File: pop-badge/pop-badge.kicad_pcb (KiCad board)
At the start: 2 copper layers, 129.5 x 101.3 mm, 164 parts, among them J1 Conn_01x05, Q1 S9013, Q2 AO3400A, U1 WS2812-2020, U10 WS2812-2020, U11 WS2812-2020, U12 WS2812-2020, U13 WS2812-2020, U14 WS2812-2020, U15 WS2812-2020, U16 WS2812-2020, U17 WS2812-2020, U18 WS2812-2020, U19 WS2812-2020, U2 WS2812-2020, U20 WS2812-2020, U21 WS2812-2020, U22 WS2812-2020, U23 WS2812-2020, U24 WS2812-2020, U25 WS2812-2020, U26 Pico, U3 WS2812-2020, U4 WS2812-2020, U5 WS2812-2020, U6 WS2812-2020, U7 WS2812-2020, U8 WS2812-2020, U9 WS2812-2020

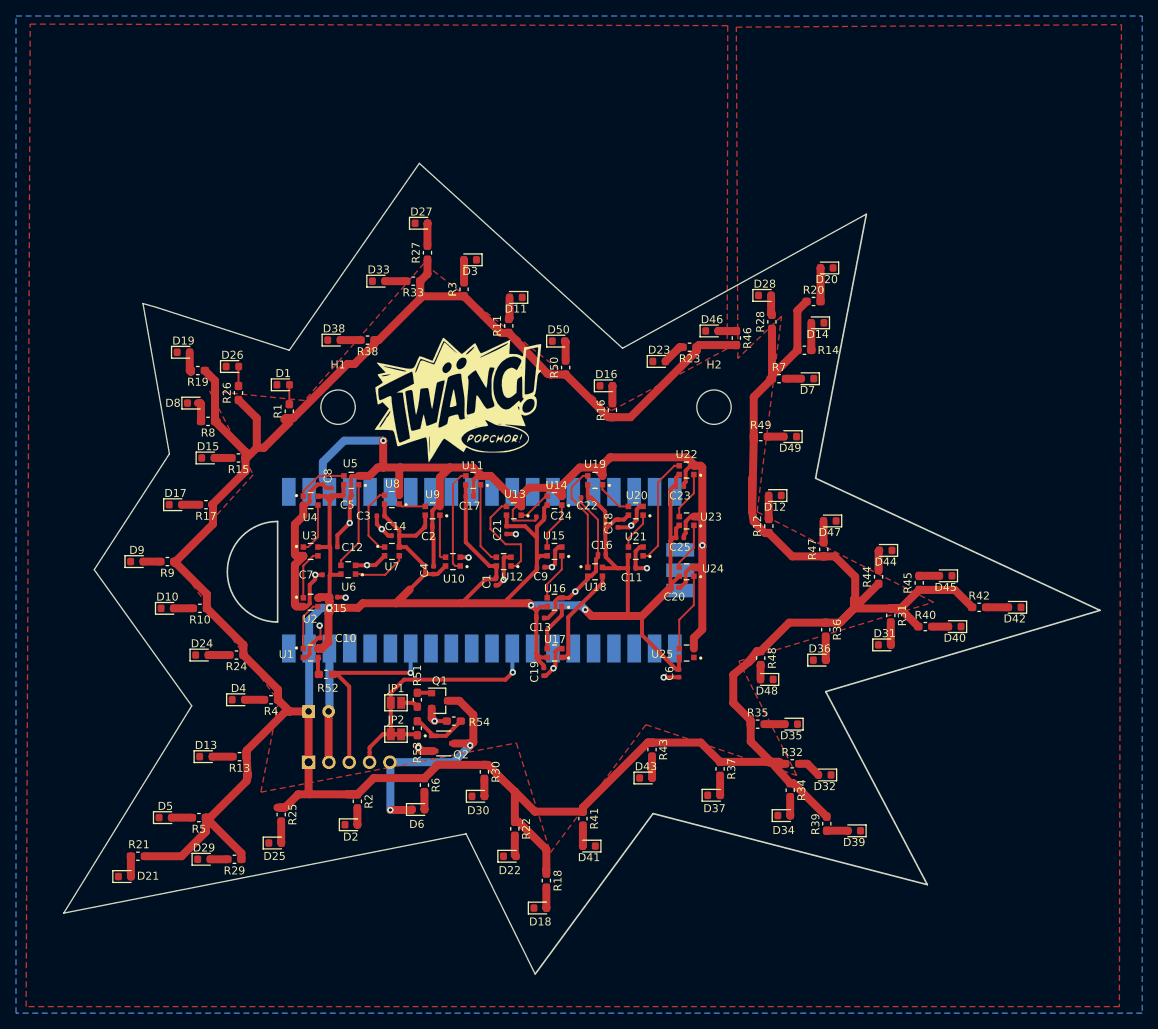
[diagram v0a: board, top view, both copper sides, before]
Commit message: add button
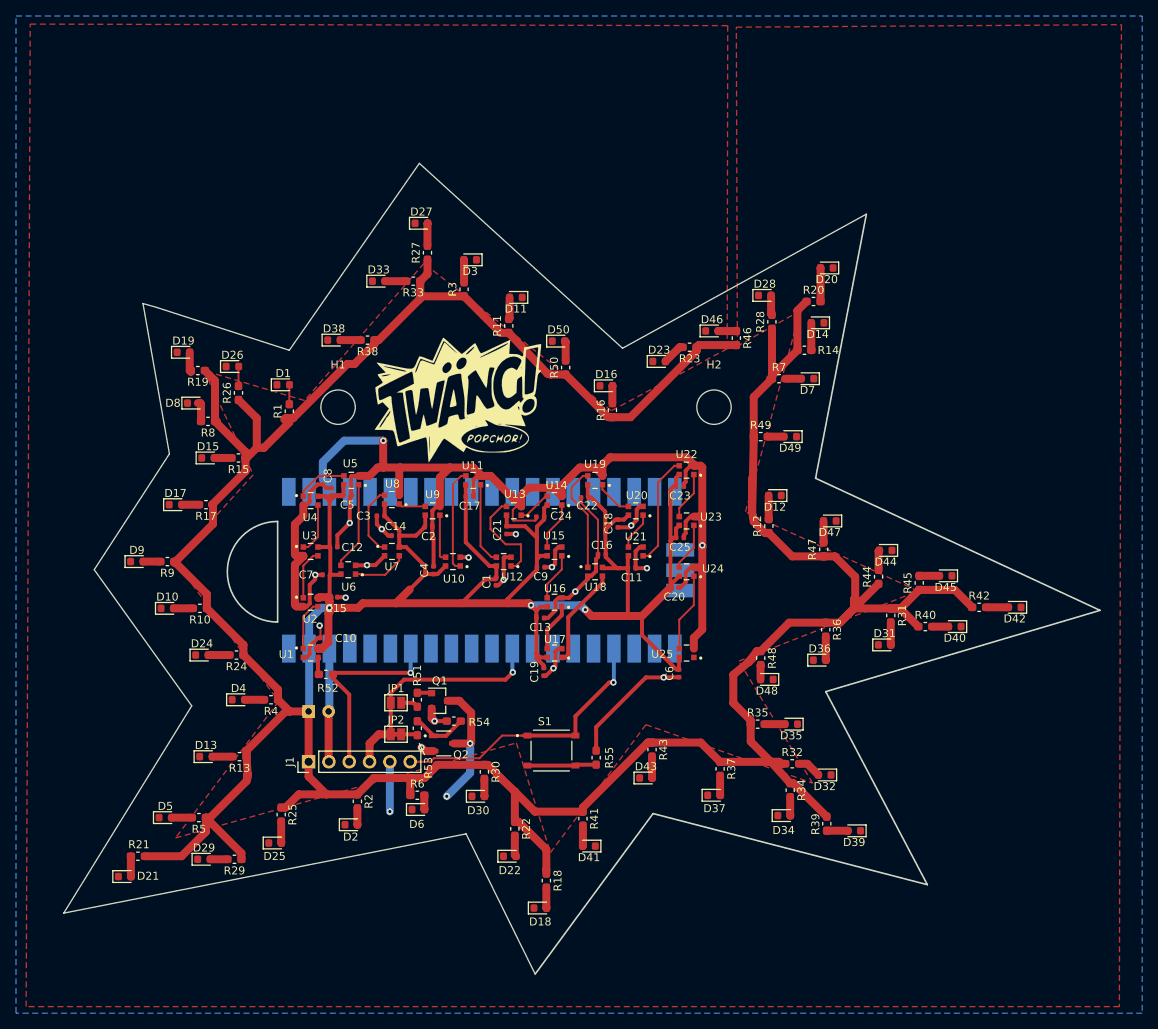
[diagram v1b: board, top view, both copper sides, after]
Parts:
- added R55: 200, Resistor_SMD:R_0603_1608Metric_Pad1.05x0.95mm_HandSolder, F.Cu at (80.5, 116.2)
- added S1: TS-1187A-B-A-B, footprints:SW_TS-1187A-B-A-B, F.Cu at (74.9, 115.3)
- J1: value Conn_01x05 -> Conn_01x06; footprint Connector_PinSocket_2.54mm:PinSocket_1x05_P2.54mm_Vertical -> Connector_PinHeader_2.54mm:PinHeader_1x06_P2.54mm_Vertical; moved to F.Cu
- Raspberry Pi Pico: renamed from U26
- moved R6 1.55 mm to (58.2, 120.9), turned to 0 degrees
- moved J1 0.06 mm to (44.6, 116.7), turned to 90 degrees
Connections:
- Raspberry Pi Pico pad 24: Net-(U26-Pad24) -> Button
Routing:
- net Button: track 0.00 -> 36.8 mm, vias 0 -> 1
- net GND: track 248.7 -> 262.8 mm
- net Net-(R55-Pad1): track 0.00 -> 8.63 mm
- net LEDw-: track 29.7 -> 23.5 mm, vias 2 -> 3
- net +5V: track 642.3 -> 644.1 mm
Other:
- board text added: "Button"
- board text added: "jlcjlcjlcjlcjlcjlc"

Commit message: some cosmetic changes
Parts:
- U26: renamed from Raspberry Pi Pico
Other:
- board text added: "JLCJLCJLCJLC"
- board text removed: "jlcjlcjlcjlcjlcjlc"
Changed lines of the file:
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@@
     (tags "Through hole pin header THT 2x20 2.54mm double row")
     (attr smd)
-    (fp_text reference "Raspberry Pi Pico" (at -0.9525 -14.1605 180) (layer B.SilkS)
+    (fp_text reference U26 (at -0.9525 -14.1605 180) (layer B.SilkS)
       (effects (font (size 1 1) (thickness 0.15)) (justify mirror))
     )
@@
     )
   )
-  (gr_text jlcjlcjlcjlcjlcjlc (at 51.181 89.916) (layer B.SilkS)
+  (gr_text JLCJLCJLCJLC (at 51.181 89.916) (layer B.SilkS)
     (effects (font (size 1 1) (thickness 0.15)) (justify mirror))
   )

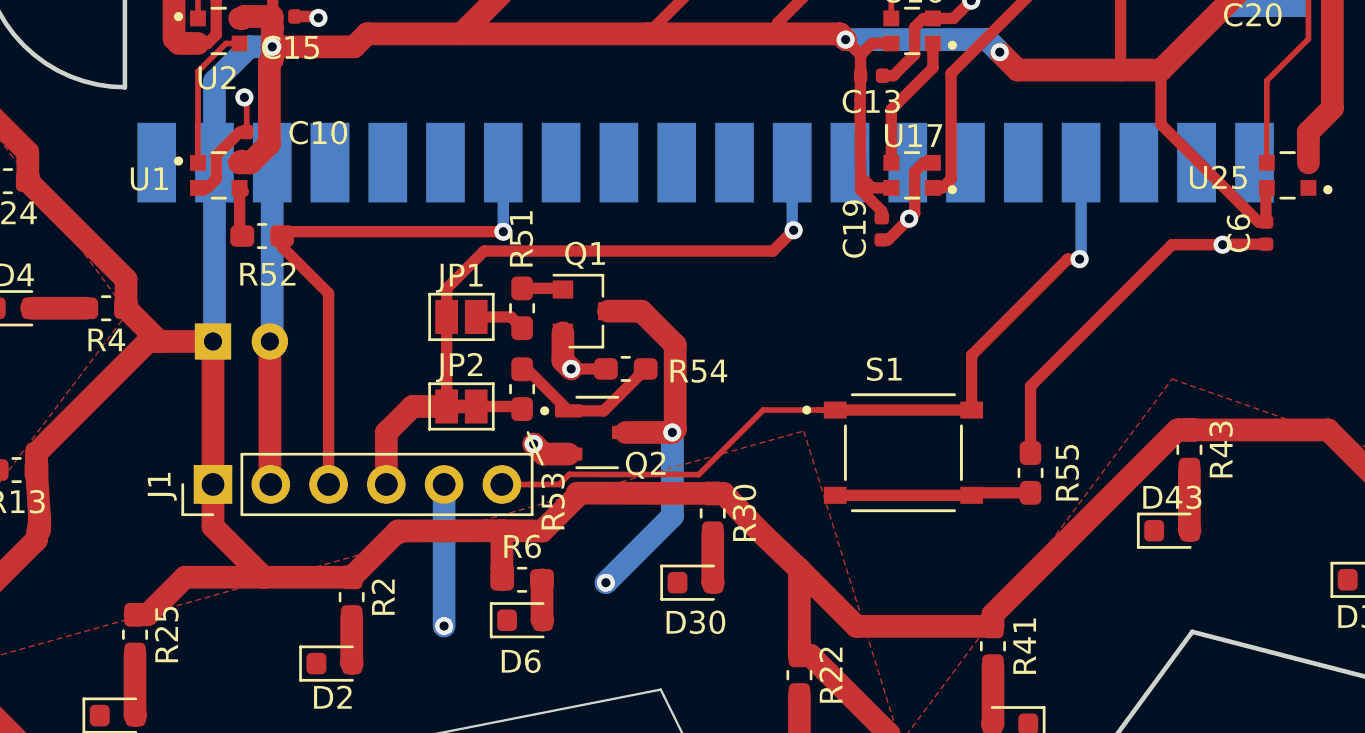
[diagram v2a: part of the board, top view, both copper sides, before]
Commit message: remove button again
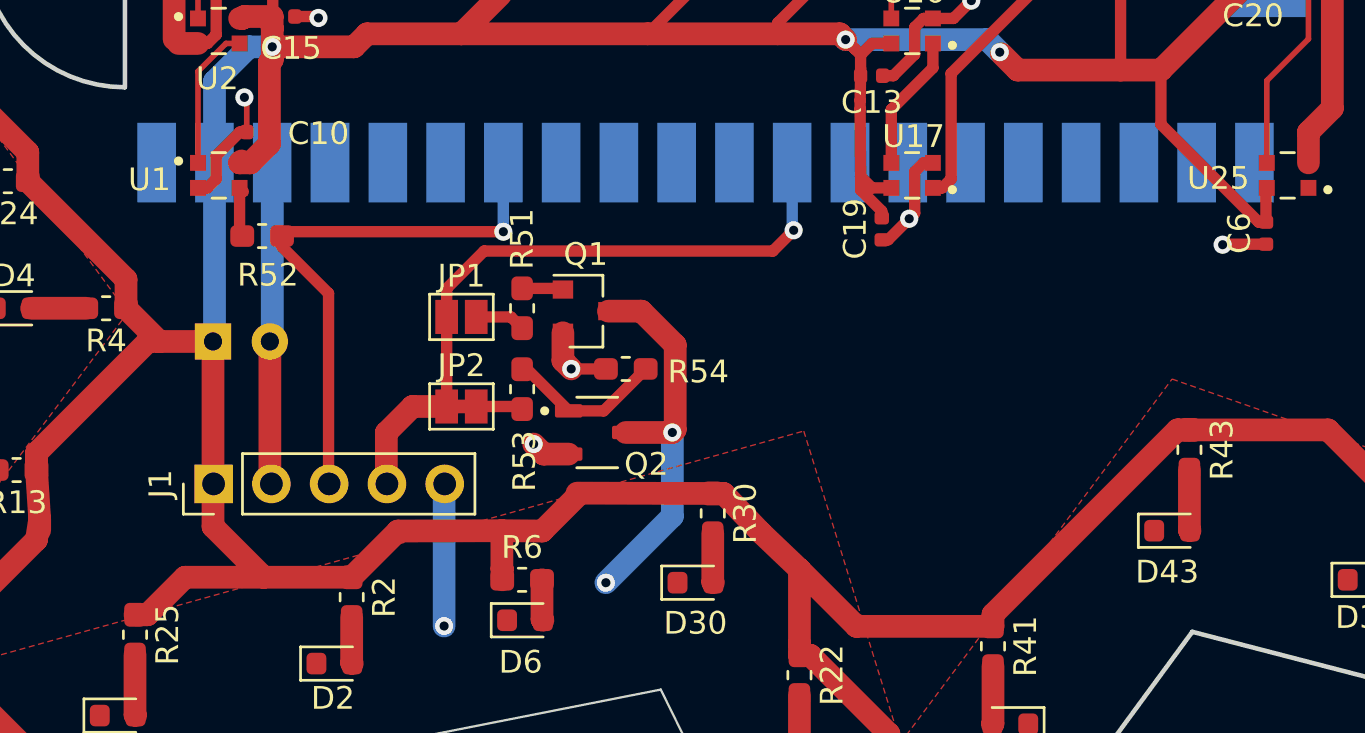
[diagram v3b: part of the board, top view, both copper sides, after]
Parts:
- removed R55: 200, Resistor_SMD:R_0603_1608Metric_Pad1.05x0.95mm_HandSolder
- removed S1: TS-1187A-B-A-B, footprints:SW_TS-1187A-B-A-B
- J1: value Conn_01x06 -> Conn_01x05; footprint Connector_PinHeader_2.54mm:PinHeader_1x06_P2.54mm_Vertical -> Connector_PinHeader_2.54mm:PinHeader_1x05_P2.54mm_Vertical
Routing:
- net Button: track 36.8 -> 0.00 mm, vias 1 -> 0
- net GND: track 262.8 -> 248.3 mm
- net Net-(R55-Pad1): track 8.63 -> 0.00 mm

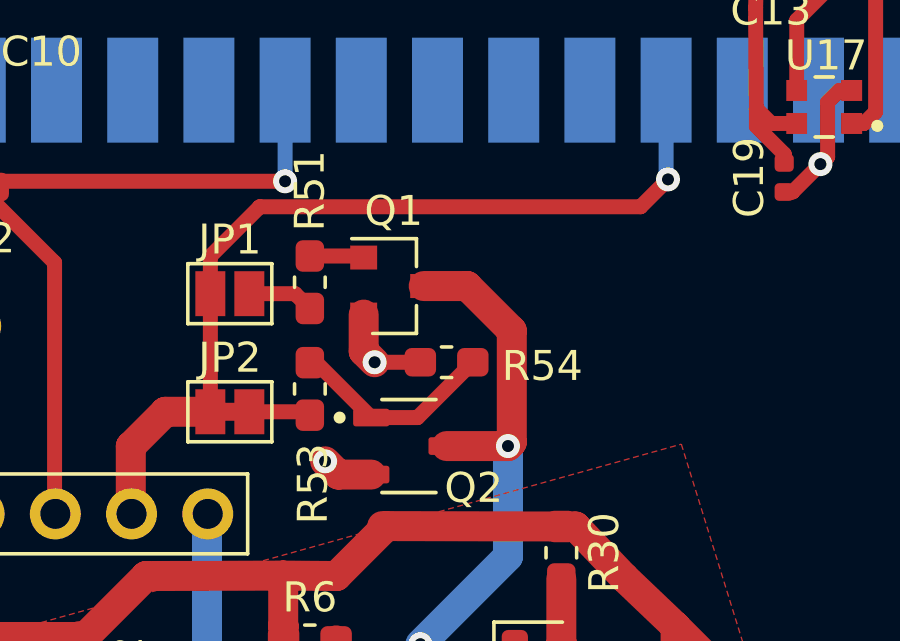
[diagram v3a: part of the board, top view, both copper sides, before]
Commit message: change footprint for npn slightly
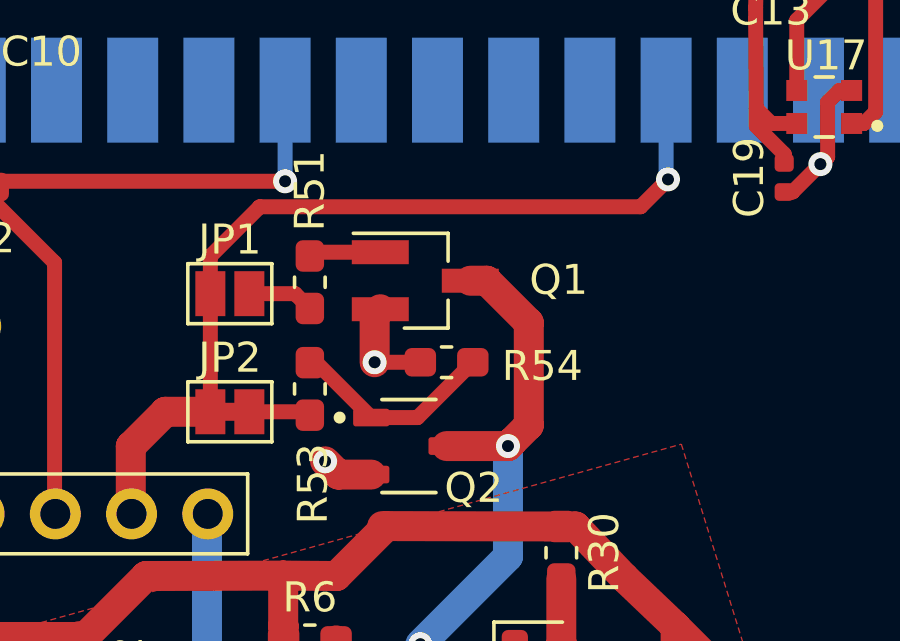
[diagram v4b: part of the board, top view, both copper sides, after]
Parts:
- Q1: footprint Package_TO_SOT_SMD:SOT-23 -> Package_TO_SOT_SMD:SOT-23_Handsoldering
- moved Q1 1.07 mm to (62.0, 108.9)
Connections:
- net Button renamed Net-(U26-Pad24)
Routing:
- net Net-(Q1-Pad1): track 1.82 -> 2.40 mm
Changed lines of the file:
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@@
     (thickness 1.6)
     (drawings 27)
-    (tracks 736)
+    (tracks 737)
     (zones 0)
     (modules 164)
@@
     (47 F.CrtYd user)
     (48 B.Fab user)
-    (49 F.Fab user)
+    (49 F.Fab user hide)
   )
   (setup
-    (last_trace_width 1)
+    (last_trace_width 0.5)
     (user_trace_width 0.25)
     (user_trace_width 0.5)
@@
   (net 121 "Net-(JP2-Pad2)")
   (net 122 "Net-(Q2-Pad1)")
-  (net 123 Button)
+  (net 123 "Net-(U26-Pad24)")
   (net_class Default "This is the default net class."
     (clearance 0.2)
@@
     (uvia_drill 0.1)
     (add_net +5V)
-    (add_net Button)
     (add_net DIN)
     (add_net GND)
@@
     (add_net "Net-(U26-Pad22)")
     (add_net "Net-(U26-Pad23)")
+    (add_net "Net-(U26-Pad24)")
     (add_net "Net-(U26-Pad25)")
     (add_net "Net-(U26-Pad26)")
@@
     (add_net "Net-(U8-Pad1)")
   )
+  (module Package_TO_SOT_SMD:SOT-23_Handsoldering (layer F.Cu)
+    (at 62.0141 108.9152)
+    (descr "SOT-23, Handsoldering")
+    (tags SOT-23)
+    (attr smd)
+    (fp_text reference Q1 (at 4.445 -0.0254) (layer F.SilkS)
+      (effects (font (size 1 1) (thickness 0.15)))
+    )
+    (fp_text value S9013 (at 0 2.5) (layer F.Fab)
+      (effects (font (size 1 1) (thickness 0.15)))
+    )
+    (fp_line (start 0.76 1.58) (end -0.7 1.58) (layer F.SilkS) (width 0.12))
+    (fp_line (start -0.7 1.52) (end 0.7 1.52) (layer F.Fab) (width 0.1))
+    (fp_line (start 0.7 -1.52) (end 0.7 1.52) (layer F.Fab) (width 0.1))
+    (fp_line (start -0.7 -0.95) (end -0.15 -1.52) (layer F.Fab) (width 0.1))
+    (fp_line (start -0.15 -1.52) (end 0.7 -1.52) (layer F.Fab) (width 0.1))
+    (fp_line (start -0.7 -0.95) (end -0.7 1.5) (layer F.Fab) (width 0.1))
+    (fp_line (start 0.76 -1.58) (end -2.4 -1.58) (layer F.SilkS) (width 0.12))
+    (fp_line (start -2.7 1.75) (end -2.7 -1.75) (layer F.CrtYd) (width 0.05))
+    (fp_line (start 2.7 1.75) (end -2.7 1.75) (layer F.CrtYd) (width 0.05))
+    (fp_line (start 2.7 -1.75) (end 2.7 1.75) (layer F.CrtYd) (width 0.05))
+    (fp_line (start -2.7 -1.75) (end 2.7 -1.75) (layer F.CrtYd) (width 0.05))
+    (fp_line (start 0.76 -1.58) (end 0.76 -0.65) (layer F.SilkS) (width 0.12))
+    (fp_line (start 0.76 1.58) (end 0.76 0.65) (layer F.SilkS) (width 0.12))
+    (fp_text user %R (at 0 0 90) (layer F.Fab)
+      (effects (font (size 0.5 0.5) (thickness 0.075)))
+    )
+    (pad 3 smd rect (at 1.5 0) (size 1.9 0.8) (layers F.Cu F.Paste F.Mask)
+      (net 2 LEDw-))
+    (pad 2 smd rect (at -1.5 0.95) (size 1.9 0.8) (layers F.Cu F.Paste F.Mask)
+      (net 32 GND))
+    (pad 1 smd rect (at -1.5 -0.95) (size 1.9 0.8) (layers F.Cu F.Paste F.Mask)
+      (net 34 "Net-(Q1-Pad1)"))
+    (model ${KISYS3DMOD}/Package_TO_SOT_SMD.3dshapes/SOT-23.wrl
+      (at (xyz 0 0 0))
+      (scale (xyz 1 1 1))
+      (rotate (xyz 0 0 0))
+    )
+  )
   (module Connector_PinHeader_2.54mm:PinHeader_1x05_P2.54mm_Vertical (layer F.Cu)
     (at 44.6024 116.6876 90)
@@
       (xy -1.88617 -7.717509) (xy -1.826686 -7.789334) (xy -1.737876 -7.733648)) (layer F.SilkS) (width 0.01))
   )
-  (module Package_TO_SOT_SMD:SOT-23 (layer F.Cu)
-    (at 60.96 109.093)
-    (descr "SOT-23, Standard")
-    (tags SOT-23)
-    (attr smd)
-    (fp_text reference Q1 (at 0 -2.5) (layer F.SilkS)
-      (effects (font (size 1 1) (thickness 0.15)))
-    )
-    (fp_text value S9013 (at 0 2.5) (layer F.Fab)
-      (effects (font (size 1 1) (thickness 0.15)))
-    )
-    (fp_line (start 0.76 1.58) (end -0.7 1.58) (layer F.SilkS) (width 0.12))
-    (fp_line (start 0.76 -1.58) (end -1.4 -1.58) (layer F.SilkS) (width 0.12))
-    (fp_line (start -1.7 1.75) (end -1.7 -1.75) (layer F.CrtYd) (width 0.05))
-    (fp_line (start 1.7 1.75) (end -1.7 1.75) (layer F.CrtYd) (width 0.05))
-    (fp_line (start 1.7 -1.75) (end 1.7 1.75) (layer F.CrtYd) (width 0.05))
-    (fp_line (start -1.7 -1.75) (end 1.7 -1.75) (layer F.CrtYd) (width 0.05))
-    (fp_line (start 0.76 -1.58) (end 0.76 -0.65) (layer F.SilkS) (width 0.12))
-    (fp_line (start 0.76 1.58) (end 0.76 0.65) (layer F.SilkS) (width 0.12))
-    (fp_line (start -0.7 1.52) (end 0.7 1.52) (layer F.Fab) (width 0.1))
-    (fp_line (start 0.7 -1.52) (end 0.7 1.52) (layer F.Fab) (width 0.1))
-    (fp_line (start -0.7 -0.95) (end -0.15 -1.52) (layer F.Fab) (width 0.1))
-    (fp_line (start -0.15 -1.52) (end 0.7 -1.52) (layer F.Fab) (width 0.1))
-    (fp_line (start -0.7 -0.95) (end -0.7 1.5) (layer F.Fab) (width 0.1))
-    (fp_text user %R (at 0 0 90) (layer F.Fab)
-      (effects (font (size 0.5 0.5) (thickness 0.075)))
-    )
-    (pad 3 smd rect (at 1 0) (size 0.9 0.8) (layers F.Cu F.Paste F.Mask)
-      (net 2 LEDw-))
-    (pad 2 smd rect (at -1 0.95) (size 0.9 0.8) (layers F.Cu F.Paste F.Mask)
-      (net 32 GND))
-    (pad 1 smd rect (at -1 -0.95) (size 0.9 0.8) (layers F.Cu F.Paste F.Mask)
-      (net 34 "Net-(Q1-Pad1)"))
-    (model ${KISYS3DMOD}/Package_TO_SOT_SMD.3dshapes/SOT-23.wrl
-      (at (xyz 0 0 0))
-      (scale (xyz 1 1 1))
-      (rotate (xyz 0 0 0))
-    )
-  )
   (module Capacitor_SMD:C_0402_1005Metric (layer F.Cu)
     (at 90.8685 105.664 90)
@@
       (net 86 "Net-(U26-Pad23)"))
     (pad 24 smd rect (at 8.89 -16.51 270) (size 3.5 1.7) (drill (offset 0.9 0)) (layers B.Cu B.Mask)
-      (net 123 Button))
+      (net 123 "Net-(U26-Pad24)"))
     (pad 25 smd rect (at 8.89 -13.97 270) (size 3.5 1.7) (drill (offset 0.9 0)) (layers B.Cu B.Mask)
       (net 87 "Net-(U26-Pad25)"))
@@
   (via (at 54.737 122.936) (size 0.8) (drill 0.4) (layers F.Cu B.Cu) (net 2))
   (segment (start 54.737 116.713) (end 54.737 122.936) (width 1) (layer B.Cu) (net 2) (status 10))
-  (segment (start 63.41 109.093) (end 64.897 110.58) (width 1) (layer F.Cu) (net 2))
-  (segment (start 64.897 110.58) (end 64.897 114.3) (width 1) (layer F.Cu) (net 2))
-  (segment (start 61.96 109.093) (end 63.41 109.093) (width 1) (layer F.Cu) (net 2) (status 10))
   (segment (start 62.723 114.427) (end 64.77 114.427) (width 1) (layer F.Cu) (net 2) (status 10))
   (via (at 64.77 114.427) (size 0.8) (drill 0.4) (layers F.Cu B.Cu) (net 2))
@@
   (segment (start 64.77 118.11) (end 61.849 121.031) (width 1) (layer B.Cu) (net 2))
   (segment (start 64.77 114.427) (end 64.77 118.11) (width 1) (layer B.Cu) (net 2))
+  (segment (start 64.0641 108.9152) (end 63.5141 108.9152) (width 1) (layer F.Cu) (net 2))
+  (segment (start 65.4641 110.3152) (end 64.0641 108.9152) (width 1) (layer F.Cu) (net 2))
+  (segment (start 65.4641 113.7329) (end 65.4641 110.3152) (width 1) (layer F.Cu) (net 2))
+  (segment (start 64.77 114.427) (end 65.4641 113.7329) (width 1) (layer F.Cu) (net 2))
   (segment (start 50.673 124.5615) (end 50.6985 124.587) (width 1) (layer F.Cu) (net 3) (status 30))
   (segment (start 50.673 122.541) (end 50.673 124.5615) (width 1) (layer F.Cu) (net 3) (status 30))
@@
   (segment (start 47.077 116.7365) (end 47.117 116.7765) (width 1) (layer F.Cu) (net 32) (status 30))
   (via (at 60.325 111.633) (size 0.8) (drill 0.4) (layers F.Cu B.Cu) (net 32))
-  (segment (start 59.96 111.268) (end 60.325 111.633) (width 1) (layer F.Cu) (net 32))
-  (segment (start 59.96 110.043) (end 59.96 111.268) (width 1) (layer F.Cu) (net 32) (status 10))
   (segment (start 61.849 111.633) (end 60.325 111.633) (width 0.5) (layer F.Cu) (net 32) (status 10))
   (segment (start 47.077 116.673) (end 47.117 116.713) (width 1) (layer F.Cu) (net 32) (status 30))
@@
   (segment (start 59.116 115.377) (end 58.674 114.935) (width 1) (layer F.Cu) (net 32))
   (segment (start 60.213 115.377) (end 59.116 115.377) (width 1) (layer F.Cu) (net 32) (status 10))
+  (segment (start 60.325 110.0543) (end 60.5141 109.8652) (width 1) (layer F.Cu) (net 32))
+  (segment (start 60.325 111.633) (end 60.325 110.0543) (width 1) (layer F.Cu) (net 32))
   (via (at 57.3405 105.6005) (size 0.8) (drill 0.4) (layers F.Cu B.Cu) (net 33))
   (segment (start 57.3405 101.6635) (end 57.3405 105.6005) (width 0.5) (layer B.Cu) (net 33) (status 10))
@@
   (segment (start 47.611 106.266) (end 49.657 108.312) (width 0.5) (layer F.Cu) (net 33))
   (segment (start 47.611 105.791) (end 47.611 106.266) (width 0.5) (layer F.Cu) (net 33) (status 10))
-  (segment (start 59.908 108.091) (end 59.96 108.143) (width 0.5) (layer F.Cu) (net 34) (status 30))
-  (segment (start 58.166 108.091) (end 59.908 108.091) (width 0.5) (layer F.Cu) (net 34) (status 30))
+  (segment (start 58.2918 107.9652) (end 58.166 108.091) (width 0.5) (layer F.Cu) (net 34))
+  (segment (start 60.5141 107.9652) (end 58.2918 107.9652) (width 0.5) (layer F.Cu) (net 34))
   (segment (start 43.916 98.554) (end 43.916 102.574) (width 0.25) (layer F.Cu) (net 35) (status 20))
   (segment (start 45.146 97.324) (end 43.916 98.554) (width 0.25) (layer F.Cu) (net 35))
